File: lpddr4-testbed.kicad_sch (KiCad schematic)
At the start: 2 parts

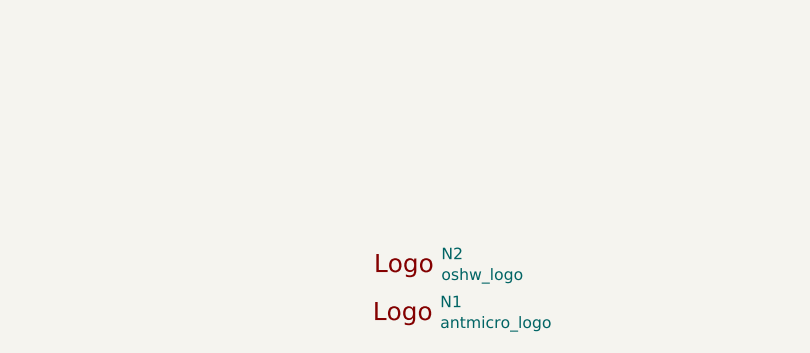
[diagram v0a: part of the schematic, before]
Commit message: Update symbols from library, redo designators
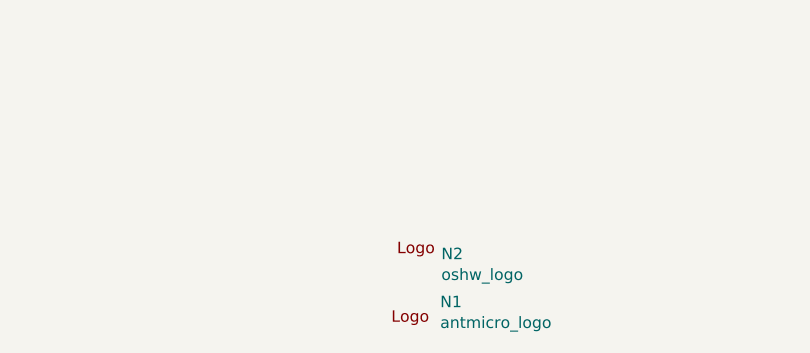
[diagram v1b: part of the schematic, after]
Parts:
- N1, N2: Author (none) -> Antmicro; License (none) -> Apache-2.0
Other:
- moved on the sheet: N1, N2
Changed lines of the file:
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@@
       (effects (font (size 1.27 1.27)) hide)
+    )
+    (property "Author" "Antmicro" (id 4) (at 125.73 280.67 0)
+      (effects (font (size 1.27 1.27) (thickness 0.15)) (justify left bottom) hide)
+    )
+    (property "License" "Apache-2.0" (id 5) (at 125.73 283.21 0)
+      (effects (font (size 1.27 1.27) (thickness 0.15)) (justify left bottom) hide)
+    )
+    (property "MPN" "" (id 6) (at 110.49 265.43 0)
+      (effects (font (size 1.27 1.27)) hide)
+    )
+    (property "Manufacturer" "" (id 7) (at 125.73 285.75 0)
+      (effects (font (size 1.27 1.27) (thickness 0.15)) (justify left bottom) hide)
     )
   )
@@
       (effects (font (size 1.27 1.27)) hide)
     )
+    (property "MPN" "" (id 4) (at 109.855 273.05 0)
+      (effects (font (size 1.27 1.27)) hide)
+    )
+    (property "Manufacturer" "" (id 5) (at 125.095 293.37 0)
+      (effects (font (size 1.27 1.27) (thickness 0.15)) (justify left bottom) hide)
+    )
+    (property "Author" "Antmicro" (id 6) (at 125.095 288.29 0)
+      (effects (font (size 1.27 1.27) (thickness 0.15)) (justify left bottom) hide)
+    )
+    (property "License" "Apache-2.0" (id 7) (at 125.095 290.83 0)
+      (effects (font (size 1.27 1.27) (thickness 0.15)) (justify left bottom) hide)
+    )
   )
